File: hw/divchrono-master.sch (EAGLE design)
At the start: 16 parts, among them U1 TPS562200DDCR

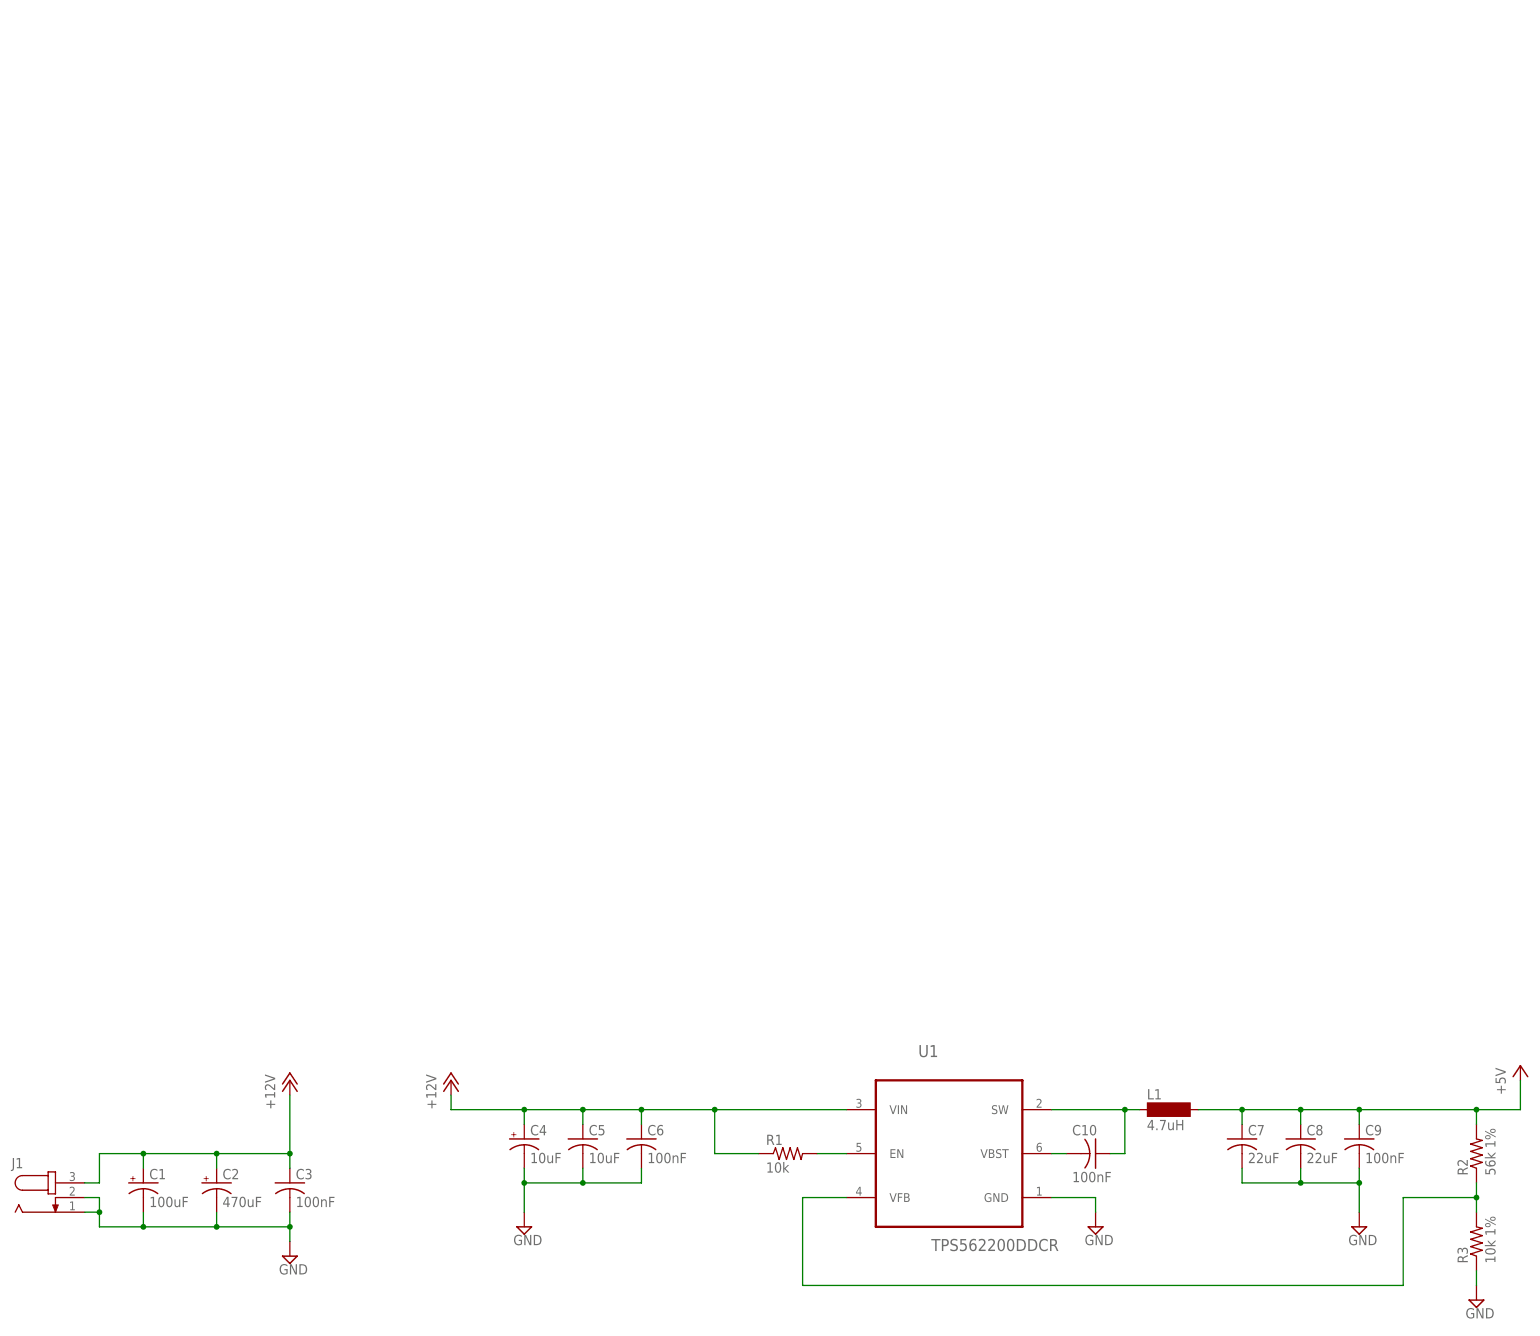
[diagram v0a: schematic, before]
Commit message: Added Nixie tube boost converter into schematic, library, and updated documentation for new layout.
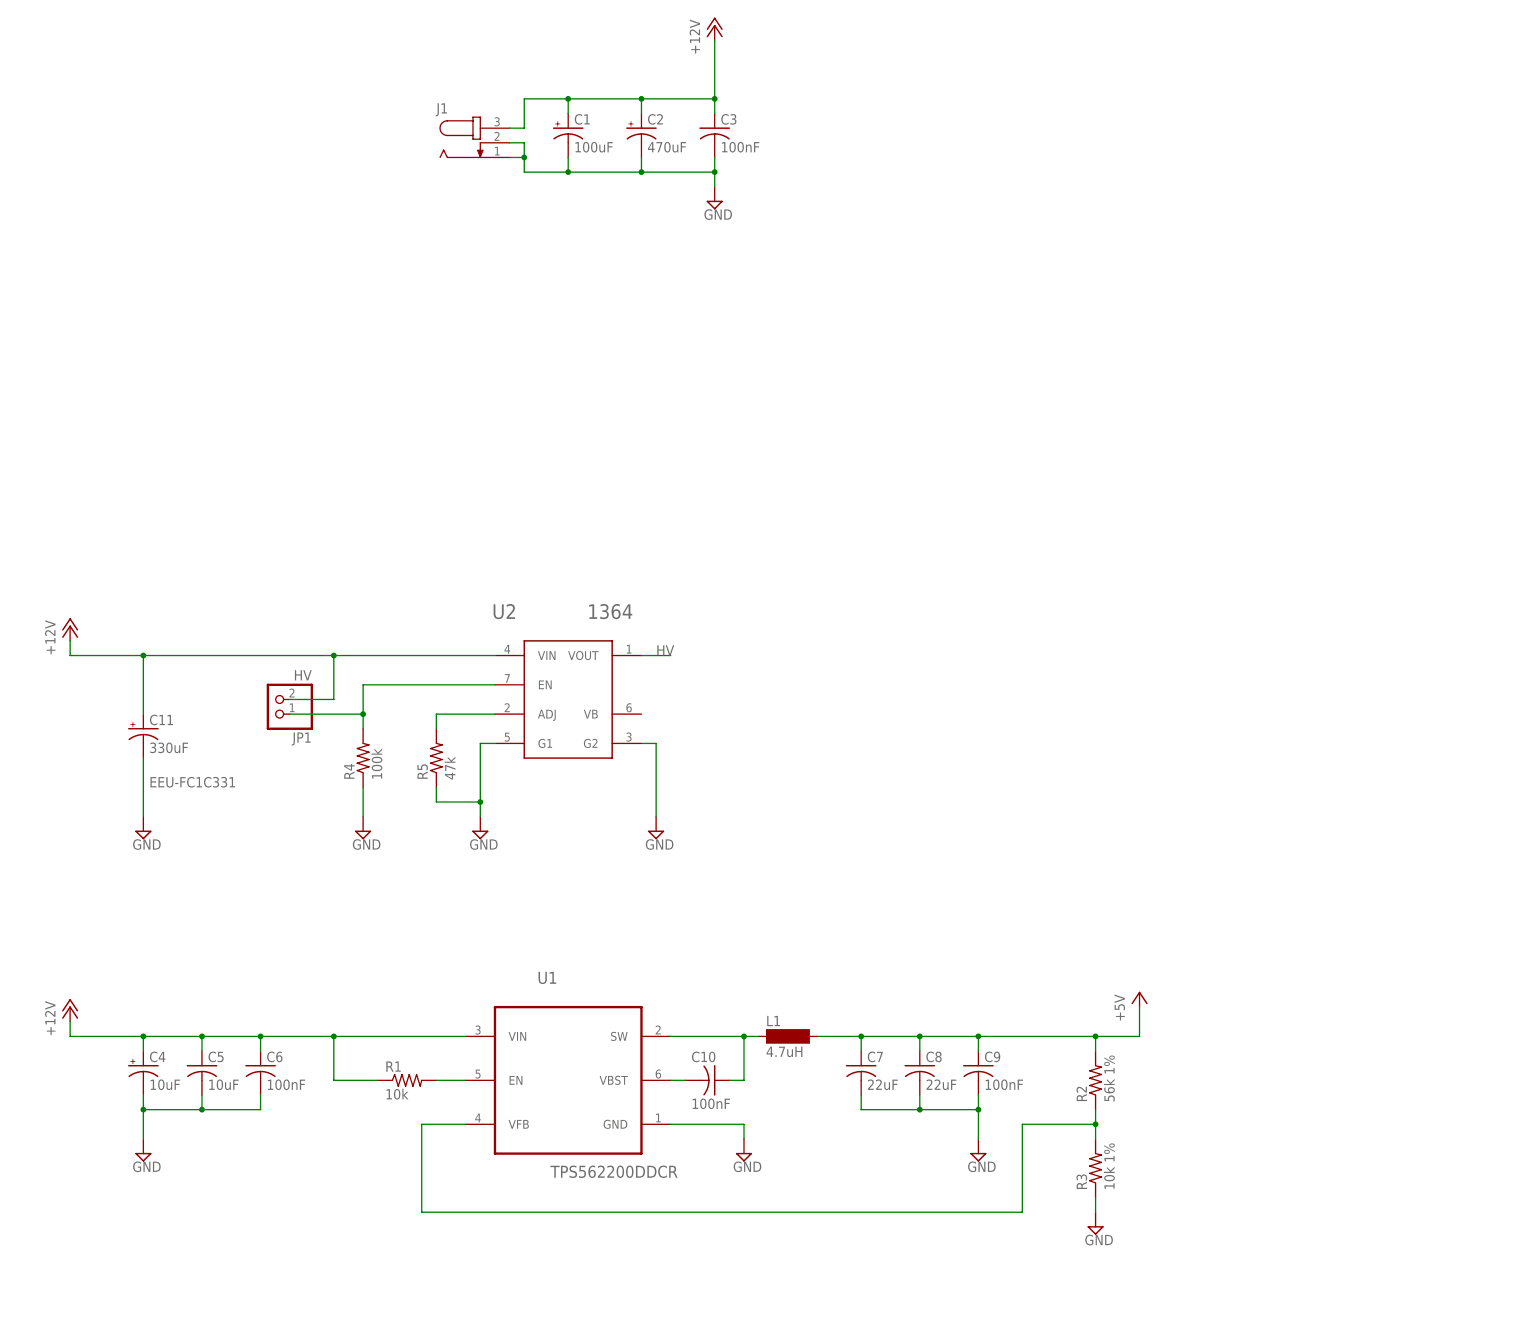
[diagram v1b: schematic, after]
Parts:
- added C11: 330uF, rcl:CPOL-USE3.5-8
- added JP1: HV, pinhead:PINHD-1X2
- added R4: 100k, rcl:R-US_R1206
- added R5: 47k, rcl:R-US_R1206
- added U2: 1364, TES:1364
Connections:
- new net HV: U2.VOUT
- new net N$3: JP1.1, R4.2, U2.EN
- new net N$4: R5.2, U2.ADJ
- net +12V: now also C11.+, JP1.2, U2.VIN
- net GND: now also C11.-, R4.1, R5.1, U2.G1, U2.G2
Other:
- note added: "EEU-FC1C331"
- moved on the sheet: C1, C10, C2, C3, C4, C5, C6, C7, C8, C9, J1, L1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

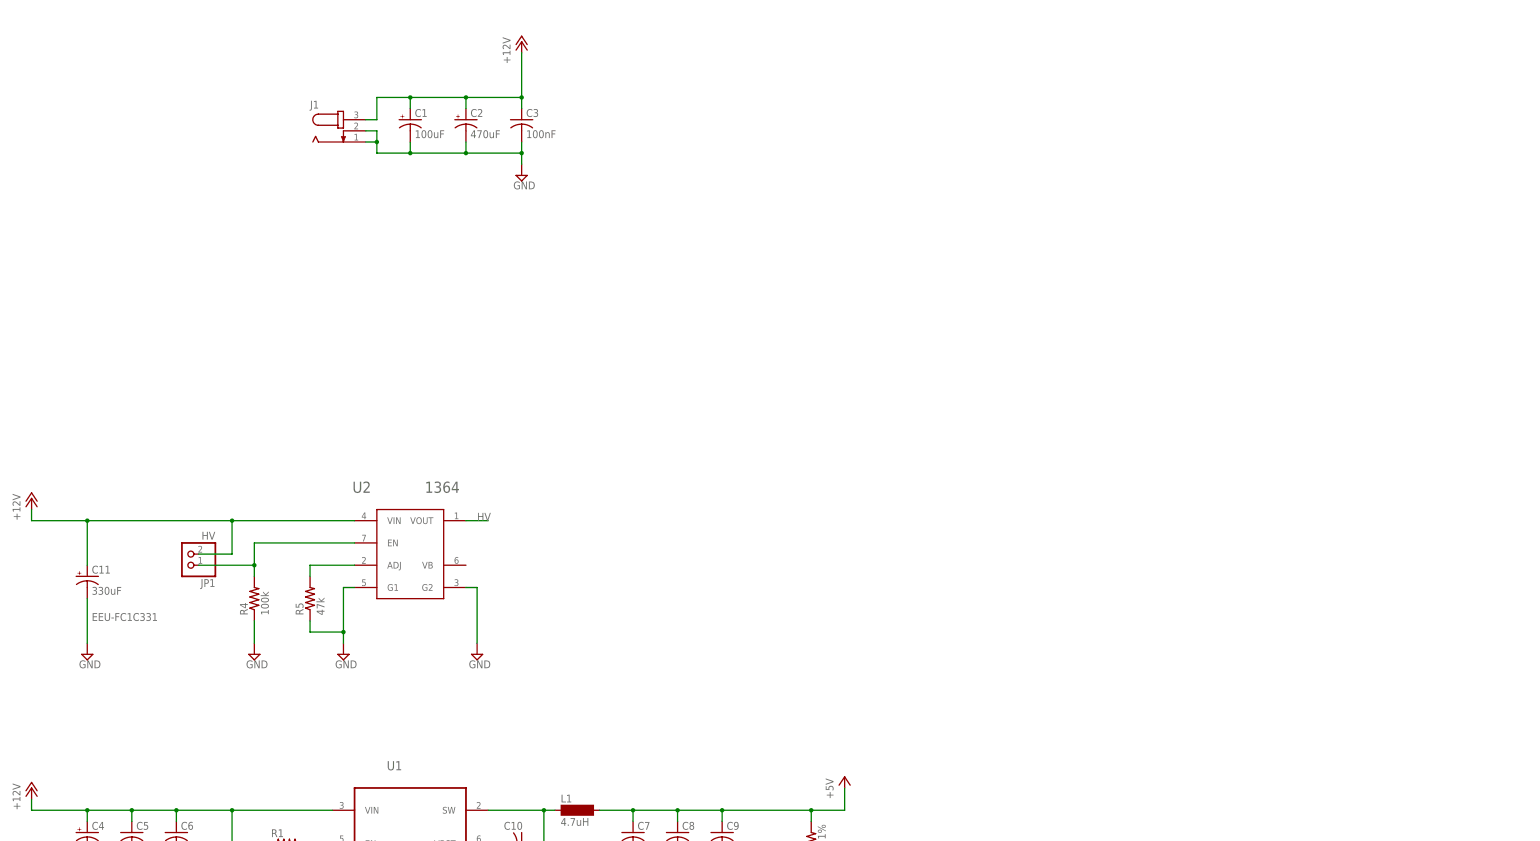
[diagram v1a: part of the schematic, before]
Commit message: Mirrored pin mappings onto schematic, and fixed two small documentation errors.
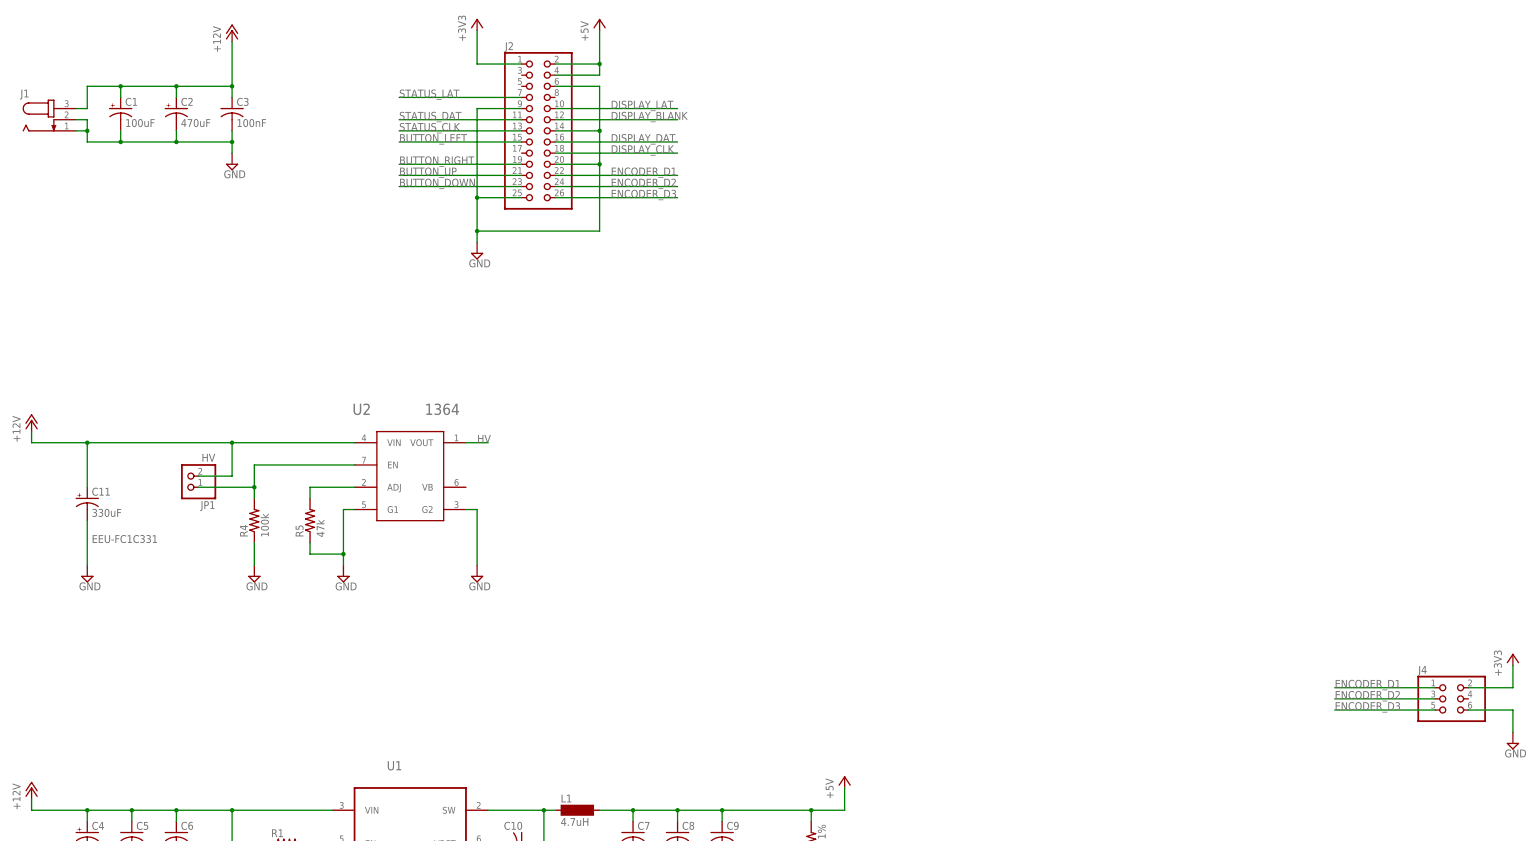
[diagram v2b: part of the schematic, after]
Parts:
- added J2: (no value), pinhead:PINHD-2X13
- added J4: (no value), pinhead:PINHD-2X3
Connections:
- new net +3V3: J2.1, J4.2
- new net BUTTON_DOWN: J2.23
- new net BUTTON_LEFT: J2.15
- new net BUTTON_RIGHT: J2.19
- new net BUTTON_UP: J2.21
- new net DISPLAY_BLANK: J2.12
- new net DISPLAY_CLK: J2.18
- new net DISPLAY_DAT: J2.16
- new net DISPLAY_LAT: J2.10
- new net ENCODER_D1: J2.22, J4.1
- new net ENCODER_D2: J2.24, J4.3
- new net ENCODER_D3: J2.26, J4.5
- new net STATUS_CLK: J2.13
- new net STATUS_DAT: J2.11
- new net STATUS_LAT: J2.7
- net +5V: now also J2.2, J2.4
- net GND: now also J2.14, J2.20, J2.25, J2.6, J2.9, J4.6
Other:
- moved on the sheet: C1, C11, C2, C3, J1, JP1, R4, R5, U2

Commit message: Laid out major board connections/pin mappings, and started on framework for encoder and amplifier boards. Minor documentation updates to reflect changes.
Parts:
- added C12, C13: 100nF, rcl:C-USC1206
- added D1, D2, D3, D4, D5, D6, D7, D8: (no value), led:LEDCHIPLED_1206
- added J3: (no value), pinhead:PINHD-2X6
- added R10, R11, R12, R13, R14, R15, R16, R17: 1k, rcl:R-US_R1206
- added R6, R7, R8, R9: 10k, rcl:R-US_R1206
- added U3: 74HC595D, 74xx-eu:74HC595D
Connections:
- new net N$10: J3.3
- new net N$11: J3.5
- new net N$12: J3.7
- new net N$13: J3.9
- new net N$14: D2.A, U3A.QB
- new net N$15: D1.A, U3A.QA
- new net N$16: D6.A, U3A.QF
- new net N$17: D7.A, U3A.QG
- new net N$18: D8.A, U3A.QH
- new net N$19: D1.C, R10.1
- new net N$20: D2.C, R11.1
- new net N$21: D3.C, R12.1
- new net N$22: D4.C, R13.1
- new net N$23: D5.C, R14.1
- new net N$24: D6.C, R15.1
- new net N$25: D7.C, R16.1
- new net N$26: D8.C, R17.1
- new net N$7: D5.A, U3A.QE
- new net N$8: D4.A, U3A.QD
- new net N$9: D3.A, U3A.QC
- net +12V: now also J3.2
- net +3V3: now also C12.1, C13.1, J2.17, R6.2, R7.2, R8.2, R9.2, U3A.SCL, U3P.VCC
- net BUTTON_DOWN: now also J3.10, R9.1
- net BUTTON_LEFT: now also J3.4, R6.1
- net BUTTON_RIGHT: now also J3.6, R7.1
- net BUTTON_UP: now also J3.8, R8.1
- net GND: now also C12.2, C13.2, J3.11, J3.12, R10.2, R11.2, R12.2, R13.2, R14.2, R15.2, R16.2, R17.2, U3A.G, U3P.GND
- net HV: now also J3.1
- net STATUS_CLK: now also U3A.SCK
- net STATUS_DAT: now also U3A.SER
- net STATUS_LAT: now also U3A.RCK
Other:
- moved on the sheet: L1

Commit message: Finished display interface and started master board schematic finalization.
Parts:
- added Q1, Q2, Q3, Q4: BSS138, SparkFun-DiscreteSemi:MOSFET-NCHANNELBSS138
- added R18, R19, R20, R21, R22, R23, R24, R25: 10k, rcl:R-US_R1206
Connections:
- removed net DISPLAY_BLANK: J2.12
- removed net DISPLAY_CLK: J2.18
- removed net DISPLAY_DAT: J2.16
- removed net DISPLAY_LAT: J2.10
- removed net N$10: J3.3
- removed net N$11: J3.5
- removed net N$12: J3.7
- removed net N$13: J3.9
- new net DISPLAY_BLANK_12V: J3.3, Q3.D, R23.1
- new net DISPLAY_BLANK_3V3: J2.12, Q3.S, R22.1
- new net DISPLAY_CLK_12V: J3.9, Q4.D, R25.1
- new net DISPLAY_CLK_3V3: J2.18, Q4.S, R24.1
- new net DISPLAY_DAT_12V: J3.7, Q2.D, R21.1
- new net DISPLAY_DAT_3V3: J2.16, Q2.S, R20.1
- new net DISPLAY_LAT_12V: J3.5, Q1.D, R19.1
- new net DISPLAY_LAT_3V3: J2.10, Q1.S, R18.1
- net +12V: now also R19.2, R21.2, R23.2, R25.2
- net +3V3: now also Q1.G, Q2.G, Q3.G, Q4.G, R18.2, R20.2, R22.2, R24.2
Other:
- moved on the sheet: C12, D1, D2, D3, D4, D5, D6, D7, D8, J3, J4, R10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

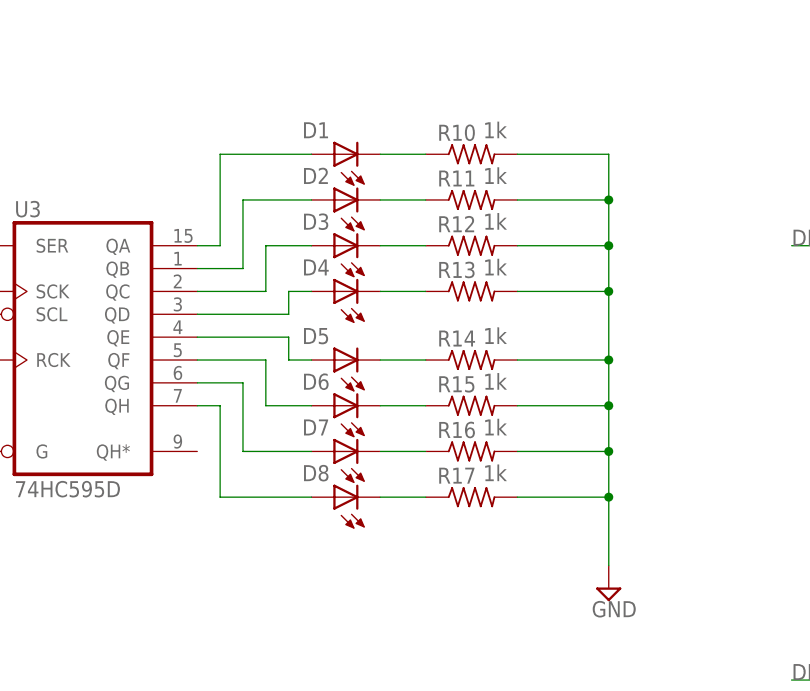
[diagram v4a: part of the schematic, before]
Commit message: Final modifications before master board layout. Changed status LED hookup to allow more streamlined part positioning.
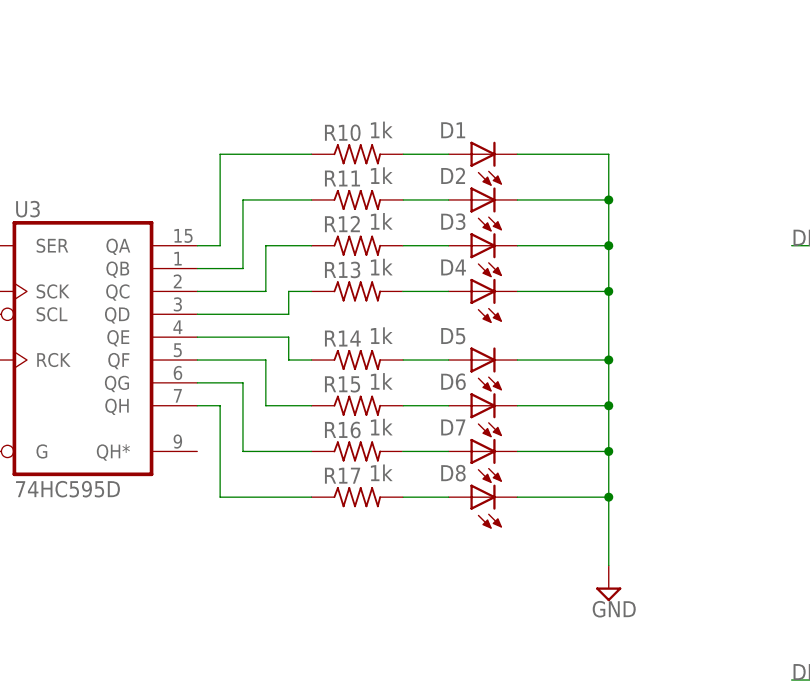
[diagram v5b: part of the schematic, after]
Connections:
- removed net N$23: D5.C, R14.1
- removed net N$24: D6.C, R15.1
- removed net N$25: D7.C, R16.1
- removed net N$26: D8.C, R17.1
- new net N$10: D8.A, R17.2
- new net N$11: D7.A, R16.2
- new net N$12: D6.A, R15.2
- new net N$13: D5.A, R14.2
- net GND: now also D1.C, D2.C, D3.C, D4.C, D5.C, D6.C, D7.C, D8.C; no longer R10.2, R11.2, R12.2, R13.2, R14.2, R15.2, R16.2, R17.2
- net N$14: now also R11.1; no longer D2.A
- net N$15: now also R10.1; no longer D1.A
- net N$16: now also R15.1; no longer D6.A
- net N$17: now also R16.1; no longer D7.A
- net N$18: now also R17.1; no longer D8.A
- net N$19: now also D4.A, R13.2; no longer D1.C, R10.1
- net N$20: now also D3.A, R12.2; no longer D2.C, R11.1
- net N$21: now also D2.A, R11.2; no longer D3.C, R12.1
- net N$22: now also D1.A, R10.2; no longer D4.C, R13.1
- net N$7: now also R14.1; no longer D5.A
- net N$8: now also R13.1; no longer D4.A
- net N$9: now also R12.1; no longer D3.A
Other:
- moved on the sheet: D1, D2, D3, D4, D5, D6, D7, D8, R10, R11, R12, R13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
